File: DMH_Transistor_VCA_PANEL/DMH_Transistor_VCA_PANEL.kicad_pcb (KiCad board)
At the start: 2 copper layers, 50 x 200 mm, 19 parts, among them J0 Panel_GND_Solder_Wire_Pad

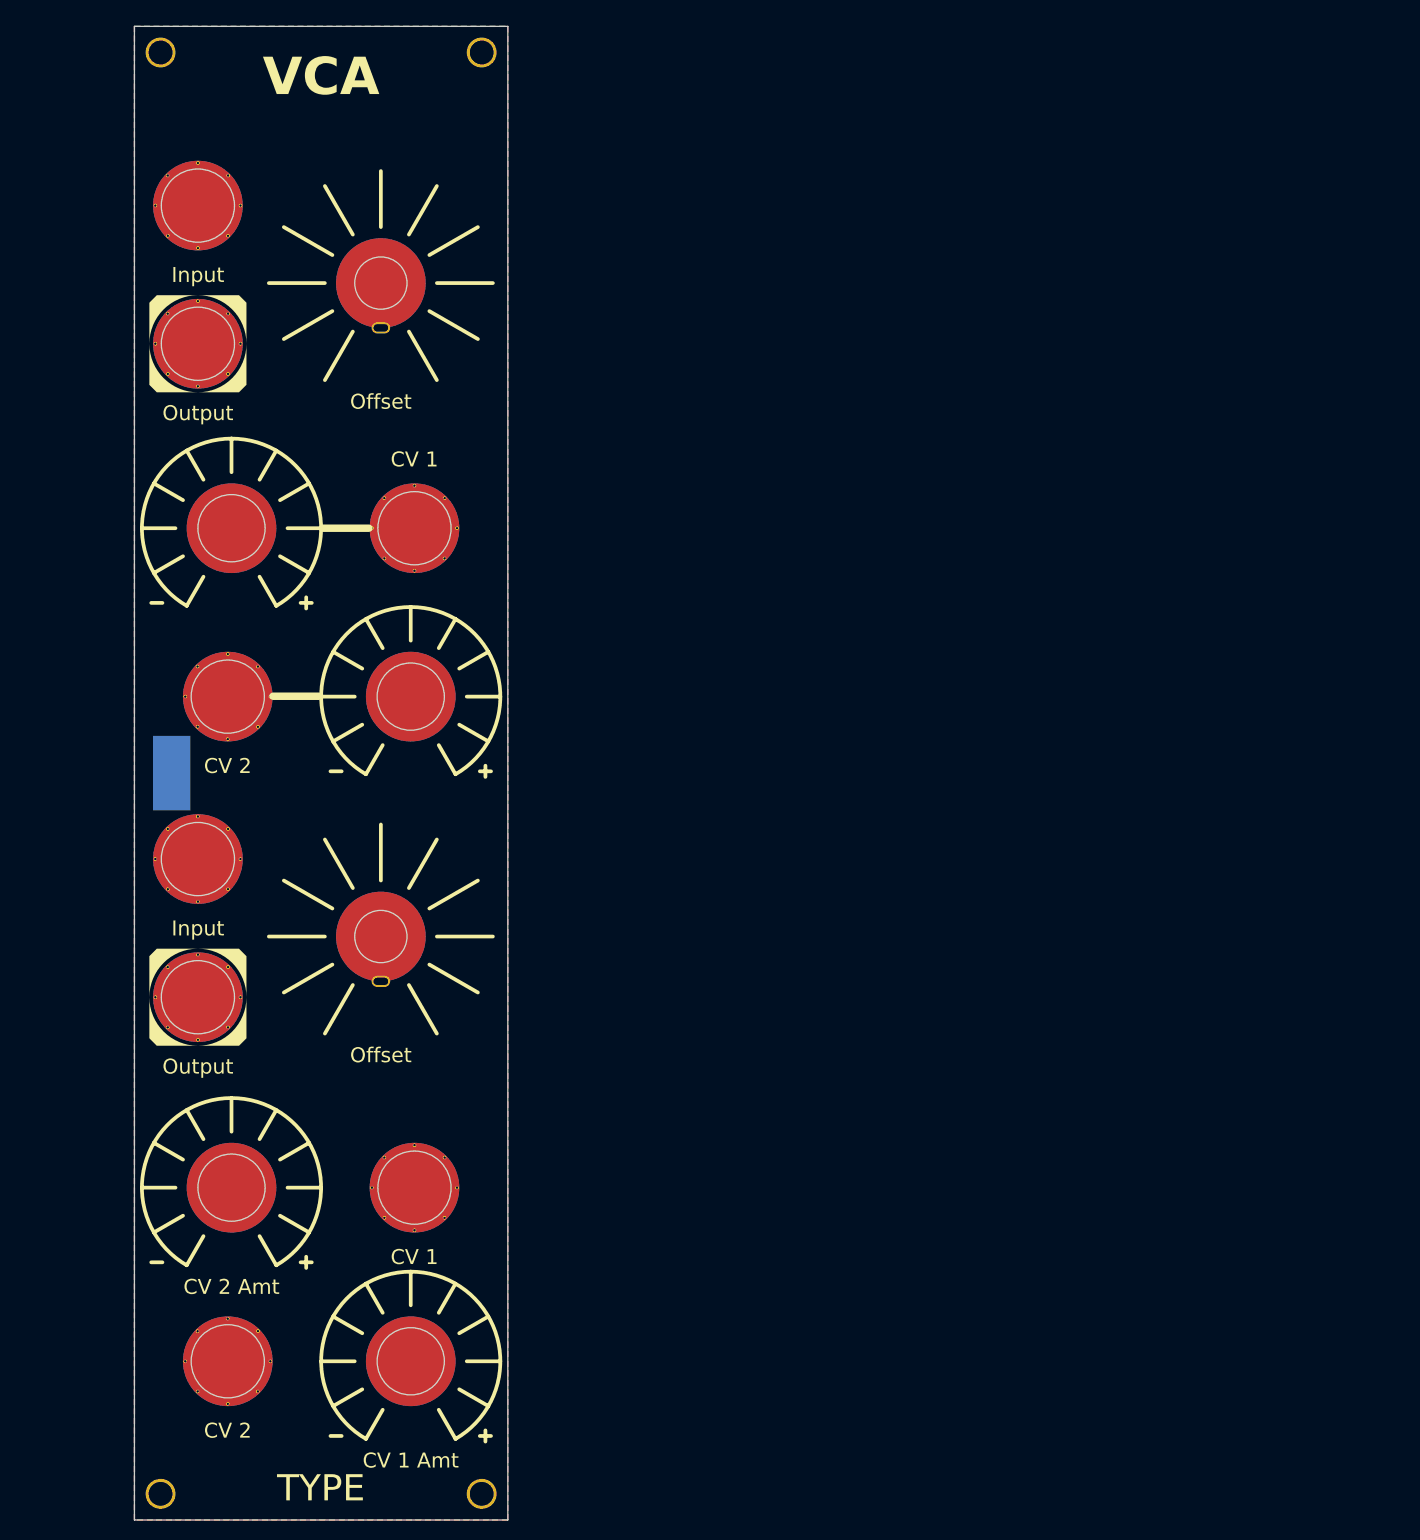
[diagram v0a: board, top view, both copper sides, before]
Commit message: Panel experiment in progress
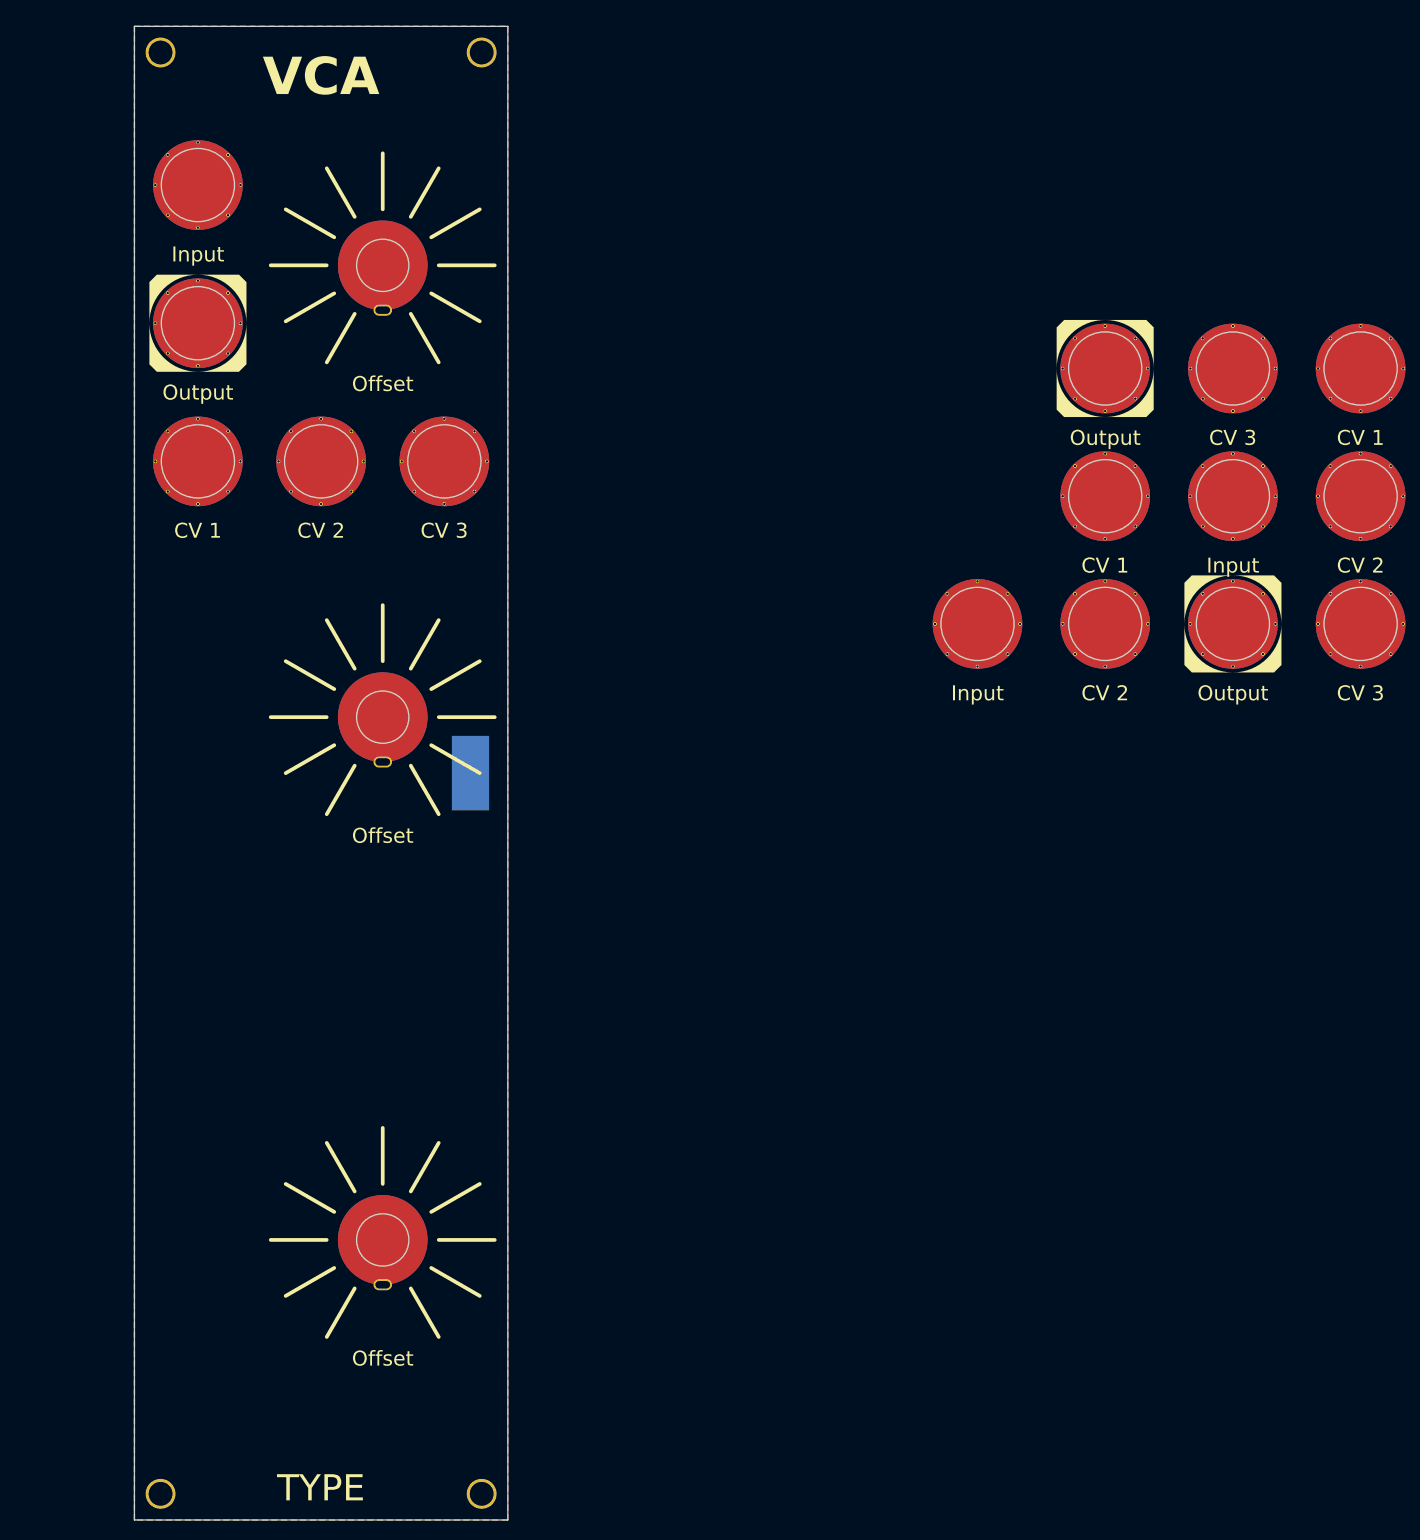
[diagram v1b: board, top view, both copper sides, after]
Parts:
- added H19: Output, SynthStuff:Jack_6.35mm_Cutout_Output_v6, F.Cu at (197.1, 110.0)
- added H20: CV 1, SynthStuff:Jack_6.35mm_Cutout_v3, F.Cu at (214.2, 75.8)
- added H21: CV 2, SynthStuff:Jack_6.35mm_Cutout_v3, F.Cu at (214.2, 92.9)
- added H22: CV 3, SynthStuff:Jack_6.35mm_Cutout_v3, F.Cu at (214.2, 110.0)
- H10: value CV 2 -> CV 3
- H11: value Output -> Offset; footprint SynthStuff:Jack_6.35mm_Cutout_Output_v6 -> SynthStuff:Pot_Cutout_Small
- H12: value Offset -> Input; footprint SynthStuff:Pot_Cutout_Small -> SynthStuff:Jack_6.35mm_Cutout_v3
- H13: value CV 1 Amt -> Output; footprint SynthStuff:Pot_Cutout_Tiny_attv -> SynthStuff:Jack_6.35mm_Cutout_Output_v6
- H14: value CV 2 Amt -> CV 1; footprint SynthStuff:Pot_Cutout_Tiny_attv -> SynthStuff:Jack_6.35mm_Cutout_v3
- H15: value Input -> CV 2
- H16: value Output -> CV 3; footprint SynthStuff:Jack_6.35mm_Cutout_Output_v6 -> SynthStuff:Jack_6.35mm_Cutout_v3
- H17: value CV 1 -> Offset; footprint SynthStuff:Jack_6.35mm_Cutout_v3 -> SynthStuff:Pot_Cutout_Small
- H18: value CV 2 -> Input
- H6: value CV 1 Amt -> Input; footprint SynthStuff:Pot_Cutout_Tiny_attv -> SynthStuff:Jack_6.35mm_Cutout_v3
- H7: value CV 2 Amt -> Output; footprint SynthStuff:Pot_Cutout_Tiny_attv -> SynthStuff:Jack_6.35mm_Cutout_Output_v6
- H8: value Input -> CV 1
- H9: value CV 1 -> CV 2
- moved H18 177.6 mm to (197.1, 92.9)
- moved H13 162.2 mm to (180.0, 75.8)
- moved H16 162.2 mm to (197.1, 75.8)
- moved H14 149.2 mm to (180.0, 92.9)
- moved H15 125.5 mm to (180.0, 110.0)
- moved H12 90.2 mm to (162.9, 110.0)
- moved H7 57.6 mm to (58.5, 69.8)
- moved H11 55.8 mm to (83.2, 122.5)
- moved H6 46.2 mm to (58.5, 51.2)
- moved H10 42.8 mm to (91.5, 88.2)
- moved J0 40.0 mm to (95.0, 130.0)
- moved H8 34.2 mm to (58.5, 88.2)
- moved H9 15.4 mm to (75.0, 88.2)
- moved H17 8.19 mm to (83.2, 192.5)
- moved H5 2.39 mm to (83.2, 62.0)

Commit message: Update DMH_Transistor_VCA_PANEL.kicad_pcb
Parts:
- moved H20 198.7 mm to (58.5, 199.2)
- moved H15 177.6 mm to (40.0, 219.2)
- moved H19 155.6 mm to (58.5, 180.8)
- moved H18 155.0 mm to (58.5, 162.2)
- moved H14 131.7 mm to (58.5, 143.8)
- moved H13 131.2 mm to (58.5, 125.2)
- moved H12 104.4 mm to (58.5, 106.8)
- moved H17 20.5 mm to (83.2, 172.0)
- moved H11 4.50 mm to (83.2, 118.0)
- moved H5 1.50 mm to (83.2, 60.5)
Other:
- board text added: "BJT-3"
- board text added: "VCM"
- board text removed: "TYPE"
- board text removed: "VCA"

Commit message: VCM studies
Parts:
- removed H10, H16, H22: CV 3, SynthStuff:Jack_6.35mm_Cutout_v3
- removed H15: CV 2, SynthStuff:Jack_6.35mm_Cutout_v3
- H14, H20, H8: value CV 1 -> CV
- H21: value CV 2 -> Mix Out -; footprint SynthStuff:Jack_6.35mm_Cutout_v3 -> SynthStuff:Jack_6.35mm_Cutout_Output_v6
- H9: value CV 2 -> Mix Out +; footprint SynthStuff:Jack_6.35mm_Cutout_v3 -> SynthStuff:Jack_6.35mm_Cutout_Output_v6
- moved H21 181.1 mm to (75.0, 208.8)
- moved H9 121.6 mm to (91.5, 208.8)
- moved H18 9.50 mm to (58.5, 171.8)
- moved H19 9.50 mm to (58.5, 190.2)
- moved H20 9.50 mm to (58.5, 208.8)
- moved H17 9.00 mm to (83.2, 181.0)
- moved H12 4.75 mm to (58.5, 111.5)
- moved H13 4.75 mm to (58.5, 130.0)
- moved H14 4.75 mm to (58.5, 148.5)
- moved H11 2.75 mm to (83.2, 120.8)
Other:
- board text added: "- Mix Out +"
